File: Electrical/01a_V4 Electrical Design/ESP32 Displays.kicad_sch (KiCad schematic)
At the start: 27 parts, among them J10 M20-8770242, J15 SSM-105-L-SV, J19 SSM-105-L-SV, U4 ESP32_S3 1.9inch AMOLED, U5 ESP32-S3 Circular AMOLED

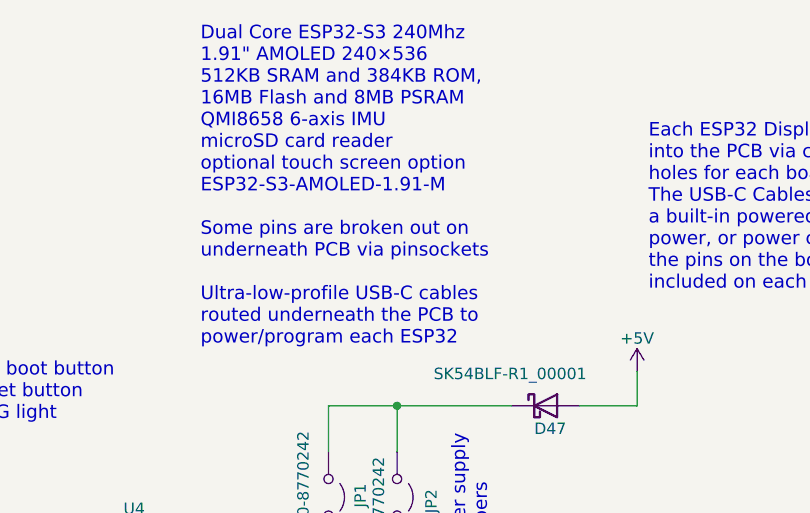
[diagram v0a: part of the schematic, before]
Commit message: main schematic tweaks. Started the 'Saber' PCB which is the new end effector for the strobe light. Schematic nearly finished. Need to create footprint for LEDs and layout the board to be CNC milled.
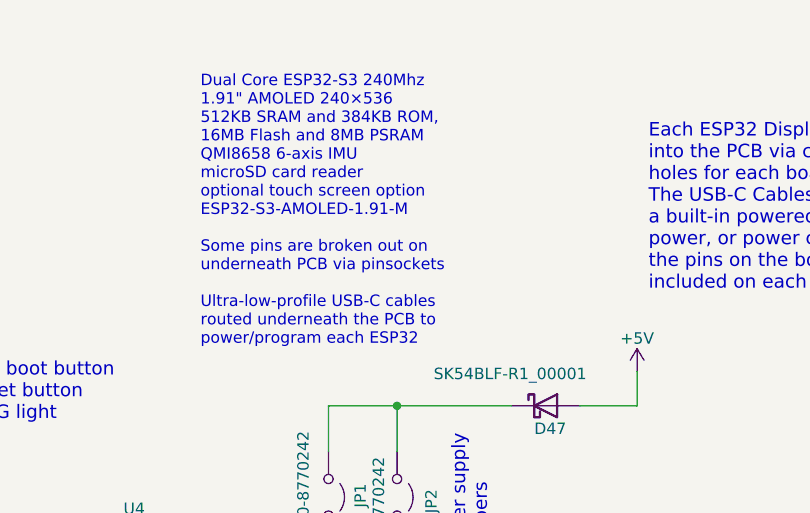
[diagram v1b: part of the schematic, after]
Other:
- company: (none) -> Kadin Whiting
- title: (none) -> ESP32 AMOLED Displays
